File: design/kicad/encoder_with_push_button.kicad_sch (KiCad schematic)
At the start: 7 parts

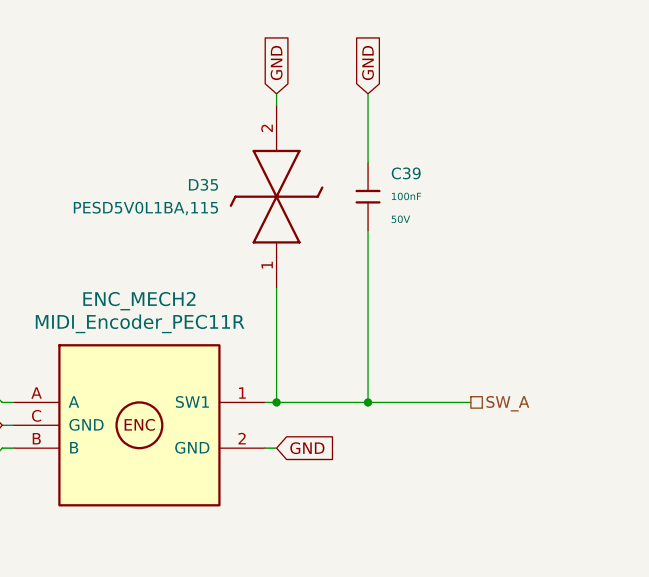
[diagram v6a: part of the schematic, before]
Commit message: Update kicad binary files
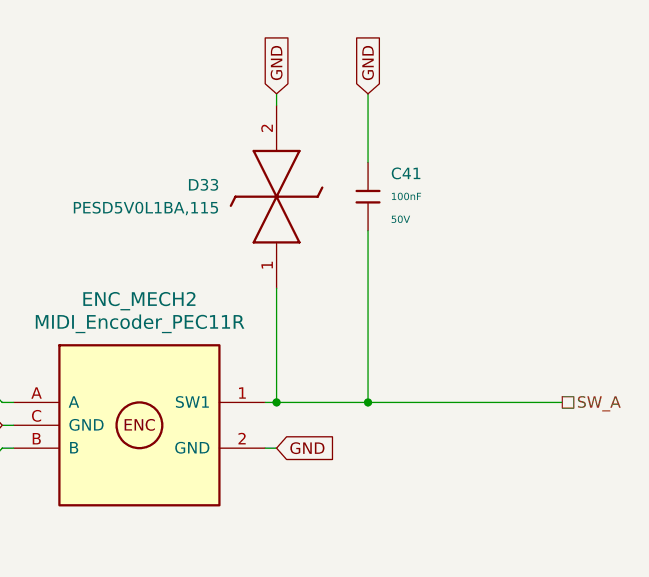
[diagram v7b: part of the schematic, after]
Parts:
- renumbered C39 to C41, D35 to D33
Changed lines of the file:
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@@
+	(wire
+		(pts
+			(xy 39.37 60.96) (xy 52.07 60.96)
+		)
+		(stroke
+			(width 0)
+			(type default)
+		)
+	)
 	(wire
 		(pts
@@
 	(wire
 		(pts
-			(xy 127 73.66) (xy 138.43 73.66)
+			(xy 127 73.66) (xy 148.59 73.66)
 		)
 		(stroke
@@
 		(pts
 			(xy 116.84 73.66) (xy 127 73.66)
-		)
-		(stroke
-			(width 0)
-			(type default)
-		)
-	)
-	(wire
-		(pts
-			(xy 39.37 60.96) (xy 52.07 60.96)
 		)
 		(stroke
@@
 	(hierarchical_label "SW_A"
 		(shape passive)
-		(at 138.43 73.66 0)
+		(at 148.59 73.66 0)
 		(effects
 			(font
@@
 			(project ""
 				(path "/9e44e663-00d0-4f33-bf1f-c4ad78deb554/f2987add-55a5-4c89-9b33-db7ed86a6cdc"
-					(reference "C2")
+					(reference "C1")
 					(unit 1)
 				)
@@
 				)
 				(path "/9e44e663-00d0-4f33-bf1f-c4ad78deb554/8b3bc88b-b526-44d8-9760-500b43fd5a71/24f763b3-d9d2-44ca-b0de-e5bd6d783cf4"
-					(reference "C18")
+					(reference "C19")
 					(unit 1)
 				)
 				(path "/9e44e663-00d0-4f33-bf1f-c4ad78deb554/8b3bc88b-b526-44d8-9760-500b43fd5a71/291f4e39-6718-4dda-83a6-20f8f943b75d"
-					(reference "C11")
+					(reference "C10")
 					(unit 1)
 				)
@@
 			(project "midi_controller"
 				(path "/9e44e663-00d0-4f33-bf1f-c4ad78deb554/f2987add-55a5-4c89-9b33-db7ed86a6cdc"
-					(reference "C1")
+					(reference "C2")
 					(unit 1)
 				)
@@
 				)
 				(path "/9e44e663-00d0-4f33-bf1f-c4ad78deb554/8b3bc88b-b526-44d8-9760-500b43fd5a71/24f763b3-d9d2-44ca-b0de-e5bd6d783cf4"
-					(reference "C19")
+					(reference "C18")
 					(unit 1)
 				)
 				(path "/9e44e663-00d0-4f33-bf1f-c4ad78deb554/8b3bc88b-b526-44d8-9760-500b43fd5a71/291f4e39-6718-4dda-83a6-20f8f943b75d"
-					(reference "C10")
+					(reference "C11")
 					(unit 1)
 				)
@@
 				)
 				(path "/9e44e663-00d0-4f33-bf1f-c4ad78deb554/8b3bc88b-b526-44d8-9760-500b43fd5a71/0ace1318-b253-4d85-b784-aa61ad0f89cd"
-					(reference "D10")
+					(reference "D11")
 					(unit 1)
 				)
 				(path "/9e44e663-00d0-4f33-bf1f-c4ad78deb554/8b3bc88b-b526-44d8-9760-500b43fd5a71/1413c73c-0ad0-4a10-833c-ff3e4825f086"
-					(reference "D19")
+					(reference "D18")
 					(unit 1)
 				)
 				(path "/9e44e663-00d0-4f33-bf1f-c4ad78deb554/8b3bc88b-b526-44d8-9760-500b43fd5a71/24f763b3-d9d2-44ca-b0de-e5bd6d783cf4"
-					(reference "D21")
+					(reference "D20")
 					(unit 1)
 				)
@@
 				)
 				(path "/9e44e663-00d0-4f33-bf1f-c4ad78deb554/8b3bc88b-b526-44d8-9760-500b43fd5a71/3c9339b8-42f1-40cb-9183-aa88346af463"
-					(reference "D15")
+					(reference "D14")
 					(unit 1)
 				)
 				(path "/9e44e663-00d0-4f33-bf1f-c4ad78deb554/8b3bc88b-b526-44d8-9760-500b43fd5a71/4af660a9-1b0e-40bf-ba48-b976c7e464d4"
-					(reference "D16")
+					(reference "D17")
 					(unit 1)
 				)
@@
 				)
 				(path "/9e44e663-00d0-4f33-bf1f-c4ad78deb554/8b3bc88b-b526-44d8-9760-500b43fd5a71/0ace1318-b253-4d85-b784-aa61ad0f89cd"
-					(reference "D11")
+					(reference "D10")
 					(unit 1)
 				)
 				(path "/9e44e663-00d0-4f33-bf1f-c4ad78deb554/8b3bc88b-b526-44d8-9760-500b43fd5a71/1413c73c-0ad0-4a10-833c-ff3e4825f086"
-					(reference "D18")
+					(reference "D19")
 					(unit 1)
 				)
 				(path "/9e44e663-00d0-4f33-bf1f-c4ad78deb554/8b3bc88b-b526-44d8-9760-500b43fd5a71/24f763b3-d9d2-44ca-b0de-e5bd6d783cf4"
-					(reference "D20")
+					(reference "D21")
 					(unit 1)
 				)
@@
 				)
 				(path "/9e44e663-00d0-4f33-bf1f-c4ad78deb554/8b3bc88b-b526-44d8-9760-500b43fd5a71/3c9339b8-42f1-40cb-9183-aa88346af463"
-					(reference "D14")
+					(reference "D15")
 					(unit 1)
 				)
 				(path "/9e44e663-00d0-4f33-bf1f-c4ad78deb554/8b3bc88b-b526-44d8-9760-500b43fd5a71/4af660a9-1b0e-40bf-ba48-b976c7e464d4"
-					(reference "D17")
+					(reference "D16")
 					(unit 1)
 				)
@@
 		(on_board yes)
 		(dnp no)
-		(property "Reference" "D35"
+		(property "Reference" "D33"
 			(at 110.49 49.5299 90)
 			(effects
@@
 				)
 				(path "/9e44e663-00d0-4f33-bf1f-c4ad78deb554/8b3bc88b-b526-44d8-9760-500b43fd5a71/0ace1318-b253-4d85-b784-aa61ad0f89cd"
+					(reference "D32")
+					(unit 1)
+				)
+				(path "/9e44e663-00d0-4f33-bf1f-c4ad78deb554/8b3bc88b-b526-44d8-9760-500b43fd5a71/1413c73c-0ad0-4a10-833c-ff3e4825f086"
+					(reference "D36")
+					(unit 1)
+				)
+				(path "/9e44e663-00d0-4f33-bf1f-c4ad78deb554/8b3bc88b-b526-44d8-9760-500b43fd5a71/24f763b3-d9d2-44ca-b0de-e5bd6d783cf4"
+					(reference "D35")
+					(unit 1)
+				)
+				(path "/9e44e663-00d0-4f33-bf1f-c4ad78deb554/8b3bc88b-b526-44d8-9760-500b43fd5a71/291f4e39-6718-4dda-83a6-20f8f943b75d"
+					(reference "D31")
+					(unit 1)
+				)
+				(path "/9e44e663-00d0-4f33-bf1f-c4ad78deb554/8b3bc88b-b526-44d8-9760-500b43fd5a71/3c9339b8-42f1-40cb-9183-aa88346af463"
+					(reference "D30")
+					(unit 1)
+				)
+				(path "/9e44e663-00d0-4f33-bf1f-c4ad78deb554/8b3bc88b-b526-44d8-9760-500b43fd5a71/4af660a9-1b0e-40bf-ba48-b976c7e464d4"
+					(reference "D37")
+					(unit 1)
+				)
+				(path "/9e44e663-00d0-4f33-bf1f-c4ad78deb554/8b3bc88b-b526-44d8-9760-500b43fd5a71/60e25267-b738-456c-86e0-26223ee5fe23"
+					(reference "D33")
+					(unit 1)
+				)
+				(path "/9e44e663-00d0-4f33-bf1f-c4ad78deb554/8b3bc88b-b526-44d8-9760-500b43fd5a71/761c51eb-8364-4d00-98cb-27a8734a6aa5"
 					(reference "D34")
-					(unit 1)
-				)
-				(path "/9e44e663-00d0-4f33-bf1f-c4ad78deb554/8b3bc88b-b526-44d8-9760-500b43fd5a71/1413c73c-0ad0-4a10-833c-ff3e4825f086"
-					(reference "D38")
-					(unit 1)
-				)
-				(path "/9e44e663-00d0-4f33-bf1f-c4ad78deb554/8b3bc88b-b526-44d8-9760-500b43fd5a71/24f763b3-d9d2-44ca-b0de-e5bd6d783cf4"
-					(reference "D37")
-					(unit 1)
-				)
-				(path "/9e44e663-00d0-4f33-bf1f-c4ad78deb554/8b3bc88b-b526-44d8-9760-500b43fd5a71/291f4e39-6718-4dda-83a6-20f8f943b75d"
-					(reference "D33")
-					(unit 1)
-				)
-				(path "/9e44e663-00d0-4f33-bf1f-c4ad78deb554/8b3bc88b-b526-44d8-9760-500b43fd5a71/3c9339b8-42f1-40cb-9183-aa88346af463"
-					(reference "D32")
-					(unit 1)
-				)
-				(path "/9e44e663-00d0-4f33-bf1f-c4ad78deb554/8b3bc88b-b526-44d8-9760-500b43fd5a71/4af660a9-1b0e-40bf-ba48-b976c7e464d4"
-					(reference "D39")
-					(unit 1)
-				)
-				(path "/9e44e663-00d0-4f33-bf1f-c4ad78deb554/8b3bc88b-b526-44d8-9760-500b43fd5a71/60e25267-b738-456c-86e0-26223ee5fe23"
-					(reference "D35")
-					(unit 1)
-				)
-				(path "/9e44e663-00d0-4f33-bf1f-c4ad78deb554/8b3bc88b-b526-44d8-9760-500b43fd5a71/761c51eb-8364-4d00-98cb-27a8734a6aa5"
-					(reference "D36")
 					(unit 1)
 				)
@@
 		(dnp no)
 		(fields_autoplaced yes)
-		(property "Reference" "C39"
+		(property "Reference" "C41"
 			(at 129.54 48.2599 0)
 			(effects
@@
 				)
 				(path "/9e44e663-00d0-4f33-bf1f-c4ad78deb554/8b3bc88b-b526-44d8-9760-500b43fd5a71/0ace1318-b253-4d85-b784-aa61ad0f89cd"
+					(reference "C40")
+					(unit 1)
+				)
+				(path "/9e44e663-00d0-4f33-bf1f-c4ad78deb554/8b3bc88b-b526-44d8-9760-500b43fd5a71/1413c73c-0ad0-4a10-833c-ff3e4825f086"
+					(reference "C44")
+					(unit 1)
+				)
+				(path "/9e44e663-00d0-4f33-bf1f-c4ad78deb554/8b3bc88b-b526-44d8-9760-500b43fd5a71/24f763b3-d9d2-44ca-b0de-e5bd6d783cf4"
+					(reference "C43")
+					(unit 1)
+				)
+				(path "/9e44e663-00d0-4f33-bf1f-c4ad78deb554/8b3bc88b-b526-44d8-9760-500b43fd5a71/291f4e39-6718-4dda-83a6-20f8f943b75d"
+					(reference "C39")
+					(unit 1)
+				)
+				(path "/9e44e663-00d0-4f33-bf1f-c4ad78deb554/8b3bc88b-b526-44d8-9760-500b43fd5a71/3c9339b8-42f1-40cb-9183-aa88346af463"
 					(reference "C38")
 					(unit 1)
 				)
-				(path "/9e44e663-00d0-4f33-bf1f-c4ad78deb554/8b3bc88b-b526-44d8-9760-500b43fd5a71/1413c73c-0ad0-4a10-833c-ff3e4825f086"
+				(path "/9e44e663-00d0-4f33-bf1f-c4ad78deb554/8b3bc88b-b526-44d8-9760-500b43fd5a71/4af660a9-1b0e-40bf-ba48-b976c7e464d4"
+					(reference "C45")
+					(unit 1)
+				)
+				(path "/9e44e663-00d0-4f33-bf1f-c4ad78deb554/8b3bc88b-b526-44d8-9760-500b43fd5a71/60e25267-b738-456c-86e0-26223ee5fe23"
+					(reference "C41")
+					(unit 1)
+				)
+				(path "/9e44e663-00d0-4f33-bf1f-c4ad78deb554/8b3bc88b-b526-44d8-9760-500b43fd5a71/761c51eb-8364-4d00-98cb-27a8734a6aa5"
 					(reference "C42")
 					(unit 1)
 				)
-				(path "/9e44e663-00d0-4f33-bf1f-c4ad78deb554/8b3bc88b-b526-44d8-9760-500b43fd5a71/24f763b3-d9d2-44ca-b0de-e5bd6d783cf4"
-					(reference "C41")
-					(unit 1)
-				)
-				(path "/9e44e663-00d0-4f33-bf1f-c4ad78deb554/8b3bc88b-b526-44d8-9760-500b43fd5a71/291f4e39-6718-4dda-83a6-20f8f943b75d"
-					(reference "C37")
-					(unit 1)
-				)
-				(path "/9e44e663-00d0-4f33-bf1f-c4ad78deb554/8b3bc88b-b526-44d8-9760-500b43fd5a71/3c9339b8-42f1-40cb-9183-aa88346af463"
-					(reference "C36")
-					(unit 1)
-				)
-				(path "/9e44e663-00d0-4f33-bf1f-c4ad78deb554/8b3bc88b-b526-44d8-9760-500b43fd5a71/4af660a9-1b0e-40bf-ba48-b976c7e464d4"
-					(reference "C43")
-					(unit 1)
-				)
-				(path "/9e44e663-00d0-4f33-bf1f-c4ad78deb554/8b3bc88b-b526-44d8-9760-500b43fd5a71/60e25267-b738-456c-86e0-26223ee5fe23"
-					(reference "C39")
-					(unit 1)
-				)
-				(path "/9e44e663-00d0-4f33-bf1f-c4ad78deb554/8b3bc88b-b526-44d8-9760-500b43fd5a71/761c51eb-8364-4d00-98cb-27a8734a6aa5"
-					(reference "C40")
-					(unit 1)
-				)
